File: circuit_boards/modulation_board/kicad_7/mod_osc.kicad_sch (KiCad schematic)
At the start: 51 parts, among them Q201 MMBT3904, SW11 E-Switch_EG2301, U6 SSI2130

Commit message: Progress on circuit boards
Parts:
- removed D?: red_green, LED_THT:LED_D5.0mm, symbol Device:LED_Dual_Bidirectional
- removed JP?: saw_pol, Jumper:SolderJumper-3_P1.3mm_Bridged12_RoundedPad1.0x1.5mm, symbol Jumper:Jumper_3_Bridged12
- removed R?: 1k2, Resistor_SMD:R_0805_2012Metric, symbol Device:R
- removed U? (x3): TL072, Package_SO:SO-8_5.3x6.2mm_P1.27mm, symbol Amplifier_Operational:TL072
- added C507: 10u, Capacitor_SMD:C_0805_2012Metric, symbol Device:C
- added R501: 1k, Resistor_SMD:R_0603_1608Metric, symbol Device:R
- added R814: 100k, Resistor_SMD:R_0603_1608Metric, symbol Device:R
- added SW11: E-Switch_EG2301B, custom_footprints:E-Switch_EG2301, symbol custom_symbols:E-Switch_EG2301
- added unit 1 of SW802
- added TP1001: MODOSC, TestPoint:TestPoint_Keystone_5000-5004_Miniature, symbol Connector:TestPoint
- added TP506: MODOSC_Vref, TestPoint:TestPoint_Keystone_5000-5004_Miniature, symbol Connector:TestPoint
- added U10 (x2): TL072, Package_SO:SOIC-8_3.9x4.9mm_P1.27mm, symbol Amplifier_Operational:TL072
- added U503: LM4040C-2.5, Package_TO_SOT_SMD:SOT-23, symbol Reference_Voltage:LM4040DBZ-2.5
- C801, C803, C804: renamed from C?; footprint Capacitor_SMD:C_0805_2012Metric -> Capacitor_SMD:C_0603_1608Metric
- R803, R804, R805, R806, R807, R808, R810, R811, R812, R813, R815, R817, R820, R821, R822, R823, R824, R825, R826, R827: renamed from R?; footprint Resistor_SMD:R_0805_2012Metric -> Resistor_SMD:R_0603_1608Metric
- R816: renamed from R?; value 200k -> 100k; footprint Resistor_SMD:R_0805_2012Metric -> Resistor_SMD:R_0603_1608Metric
- R818: renamed from R?; value 51k -> 100k; footprint Resistor_SMD:R_0805_2012Metric -> Resistor_SMD:R_0603_1608Metric
- R819: renamed from R?; value 100k -> 200k; footprint Resistor_SMD:R_0805_2012Metric -> Resistor_SMD:R_0603_1608Metric
- RV101, RV102: footprint custom_footprints:Potentiometer_P260T -> Potentiometer_THT:Potentiometer_Alpha_RD901F-40-00D_Single_Vertical
- SW11: value E-Switch_EG2301 -> E-Switch_EG2301B
- U15: renamed from U?; footprint (none) -> Package_SO:SOIC-8_3.9x4.9mm_P1.27mm
- gave numbers to parts that had none: 6
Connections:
- net +5V: now also R501.1
- net -5V: no longer R817.1
- net GND: now also C507.2, R814.1, U503.2 (A)
- net at R815.1, U6.28 (square_out): now also U15.5 (+); no longer U15.3 (+)
- net at Q201.2 (E), R208.1: now also U6.17 (hard_sync)
- net at C803.1, R818.2, R819.1: no longer R817.2
- net at R816.2: now also SW802.10; no longer SW802.1
- net at U12.12 (aux_1_mix): now also SW802.6; no longer SW802.2
- net at U12.13 (aux_2_mix): now also SW802.7; no longer SW802.3
- net at U12.10 (saw_mix): now also SW802.8; no longer SW802.4
- net at U12.11 (pulse_mix): now also SW802.9; no longer SW802.5
- net at R813.1: now also U6.21 (lin_freq); no longer U6.17 (hard_sync)
- net +2V5_REF renamed MODOSC_VREF
- net MODOSC_VREF: now also R817.1, C507.1, R501.2, TP506.1, U503.1 (K)
- removed net SQUARE_OUT: U15.1, U15.2 (-)
- net SWITCHED_OUT renamed MAIN_OUT
- net MAIN_OUT: now also TP1001.1
- net V_PER_OCT_IN_1 renamed 1V_PER_OCT
- net V_PER_OCT_IN_2 renamed EXPO_FM
- new net: R814.2, R817.2
- new net SQR_OUT: U15.6 (-), U15.7
- no-connect marks 3 -> 13
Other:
- note added: "Key Tracking"
- note added: "Manual Frequency"
- moved on the sheet: C804, Q201, R206, R207, R208, R813, R816, R817, R826, R827, SW11A, SW802B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

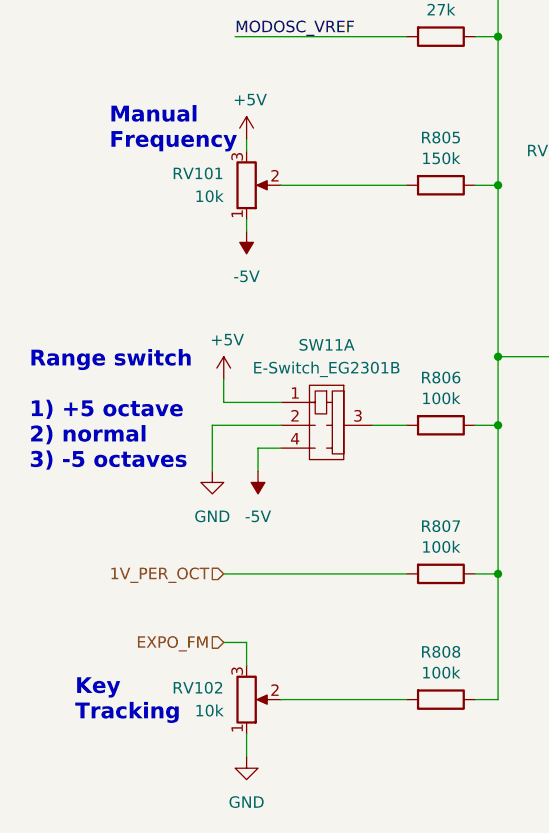
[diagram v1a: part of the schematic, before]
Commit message: Tweaks to mod board, add debug pin
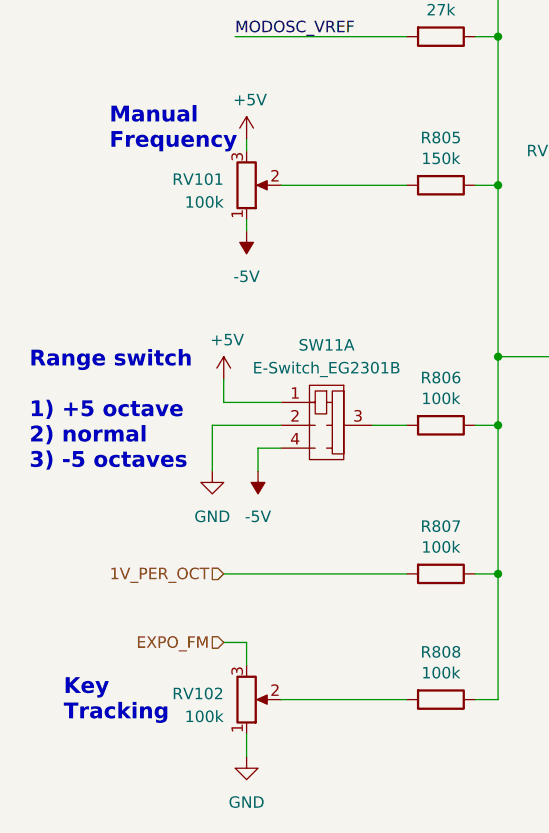
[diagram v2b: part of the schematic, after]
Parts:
- RV101, RV102: value 10k -> 100k
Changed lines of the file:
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@@
     (effects (font (size 1.75 1.75) (thickness 0.35) bold) (justify left bottom))
   )
-  (text "Key\nTracking" (at 20.32 186.69 0)
+  (text "Key\nTracking" (at 19.05 186.69 0)
     (effects (font (size 1.75 1.75) (thickness 0.35) bold) (justify left bottom))
   )
@@
   (symbol (lib_id "Device:R_Potentiometer") (at 39.37 184.15 0) (mirror x) (unit 1)
     (in_bom yes) (on_board yes) (dnp no) (fields_autoplaced)
-    (property "Reference" "RV102" (at 36.83 182.8799 0)
+    (property "Reference" "RV102" (at 36.83 183.515 0)
       (effects (font (size 1.27 1.27)) (justify right))
     )
-    (property "Value" "10k" (at 36.83 185.4199 0)
+    (property "Value" "100k" (at 36.83 186.055 0)
       (effects (font (size 1.27 1.27)) (justify right))
     )
@@
   (symbol (lib_id "Device:R_Potentiometer") (at 39.37 127 0) (mirror x) (unit 1)
     (in_bom yes) (on_board yes) (dnp no) (fields_autoplaced)
-    (property "Reference" "RV101" (at 36.83 125.7299 0)
+    (property "Reference" "RV101" (at 36.83 126.365 0)
       (effects (font (size 1.27 1.27)) (justify right))
     )
-    (property "Value" "10k" (at 36.83 128.2699 0)
+    (property "Value" "100k" (at 36.83 128.905 0)
       (effects (font (size 1.27 1.27)) (justify right))
     )

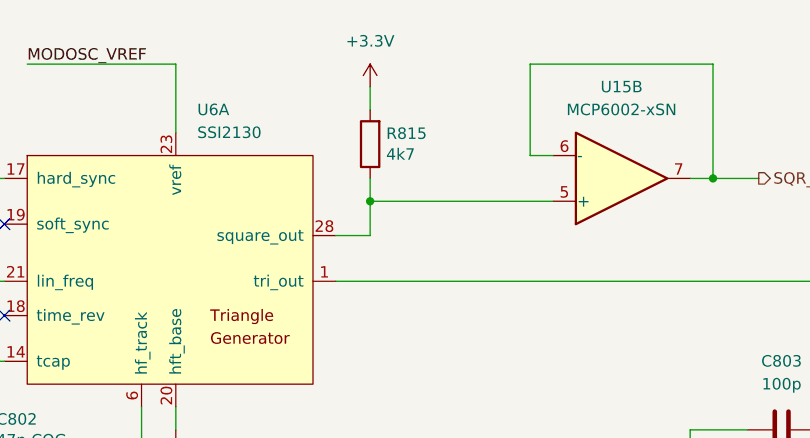
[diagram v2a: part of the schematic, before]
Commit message: Tweaks to mod board, debounce MODOSC toggle switch
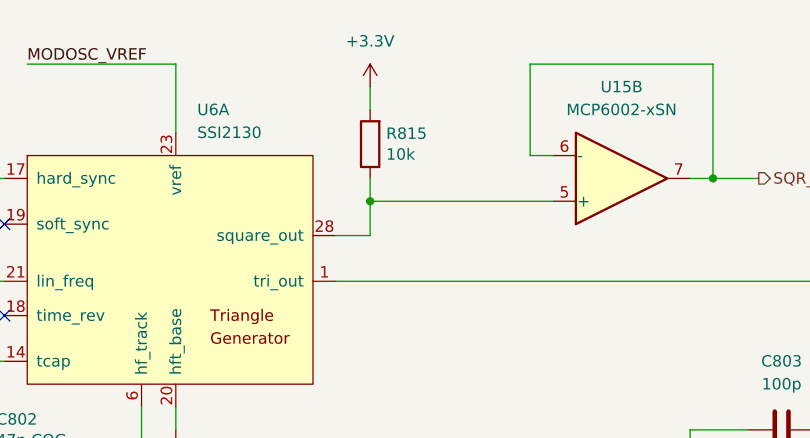
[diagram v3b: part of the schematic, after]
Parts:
- R815: value 4k7 -> 10k
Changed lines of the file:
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@@
   (title_block
     (title "MICRO-OX Modulation Board")
-    (date "2023-04-13")
+    (date "2023-04-20")
     (rev "0")
     (comment 2 "creativecommons.org/licenses/by/4.0")
@@
       (effects (font (size 1.27 1.27)) (justify right))
     )
-    (property "Value" "4k7" (at 132.588 29.083 0)
+    (property "Value" "10k" (at 132.588 29.083 0)
       (effects (font (size 1.27 1.27)) (justify right))
     )

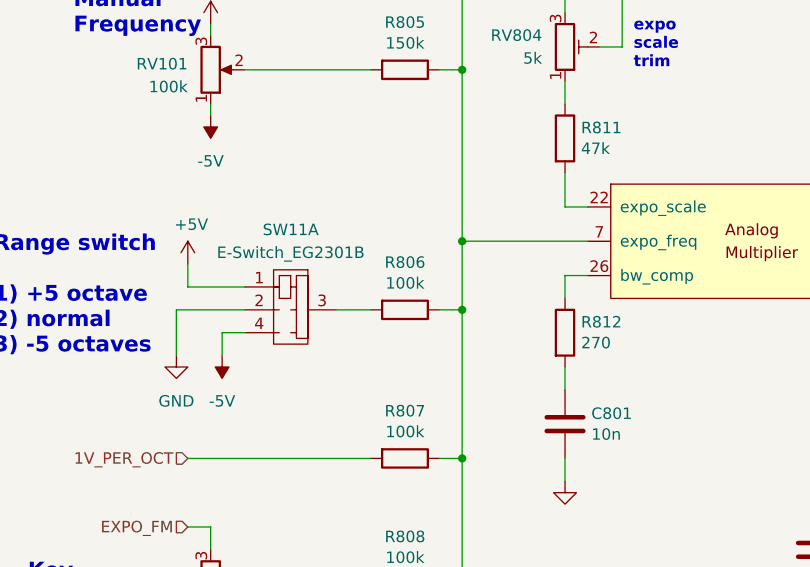
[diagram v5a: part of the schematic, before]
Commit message: Resistor tweaks while evaluating 1st build
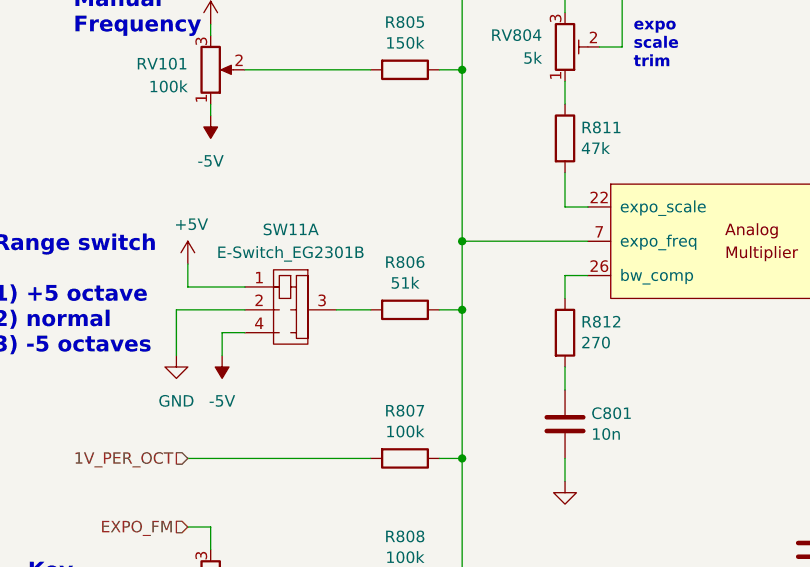
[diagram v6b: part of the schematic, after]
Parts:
- R806: value 100k -> 51k
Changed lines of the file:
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@@
       (effects (font (size 1.27 1.27)))
     )
-    (property "Value" "100k" (at 60.96 150.7236 90)
+    (property "Value" "51k" (at 60.96 150.7236 90)
       (effects (font (size 1.27 1.27)))
     )

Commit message: Add potentiometer 3d model to VCO and MOD boards
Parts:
- RV101, RV102: footprint Potentiometer_THT:Potentiometer_Alpha_RD901F-40-00D_Single_Vertical -> custom_footprints:Potentiometer_Alpha_RD901F-40-00D_Single_Vertical
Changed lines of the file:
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@@
       (effects (font (size 1.27 1.27)) (justify right))
     )
-    (property "Footprint" "Potentiometer_THT:Potentiometer_Alpha_RD901F-40-00D_Single_Vertical" (at 39.37 184.15 0)
+    (property "Footprint" "custom_footprints:Potentiometer_Alpha_RD901F-40-00D_Single_Vertical" (at 39.37 184.15 0)
       (effects (font (size 1.27 1.27)) hide)
     )
@@
       (effects (font (size 1.27 1.27)) (justify right))
     )
-    (property "Footprint" "Potentiometer_THT:Potentiometer_Alpha_RD901F-40-00D_Single_Vertical" (at 39.37 127 0)
-      (effects (font (size 1.27 1.27)) hide)
-    )
+    (property "Footprint" "custom_footprints:Potentiometer_Alpha_RD901F-40-00D_Single_Vertical" (at 39.37 127 0)
+      (effects (font (size 1.27 1.27)) hide)
+    )
